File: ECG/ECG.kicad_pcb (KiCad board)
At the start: 4 copper layers, 151.1 x 116.2 mm, 51 parts, among them J1 Conn_01x03, J2 Conn_01x03, J3 Conn_01x15, J4 Conn_01x15, J5 Conn_01x02, Q1 DMG2301L, Q2 T2N7002AK, Q3 T2N7002AK, Q4 T2N7002AK, Q5 T2N7002AK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

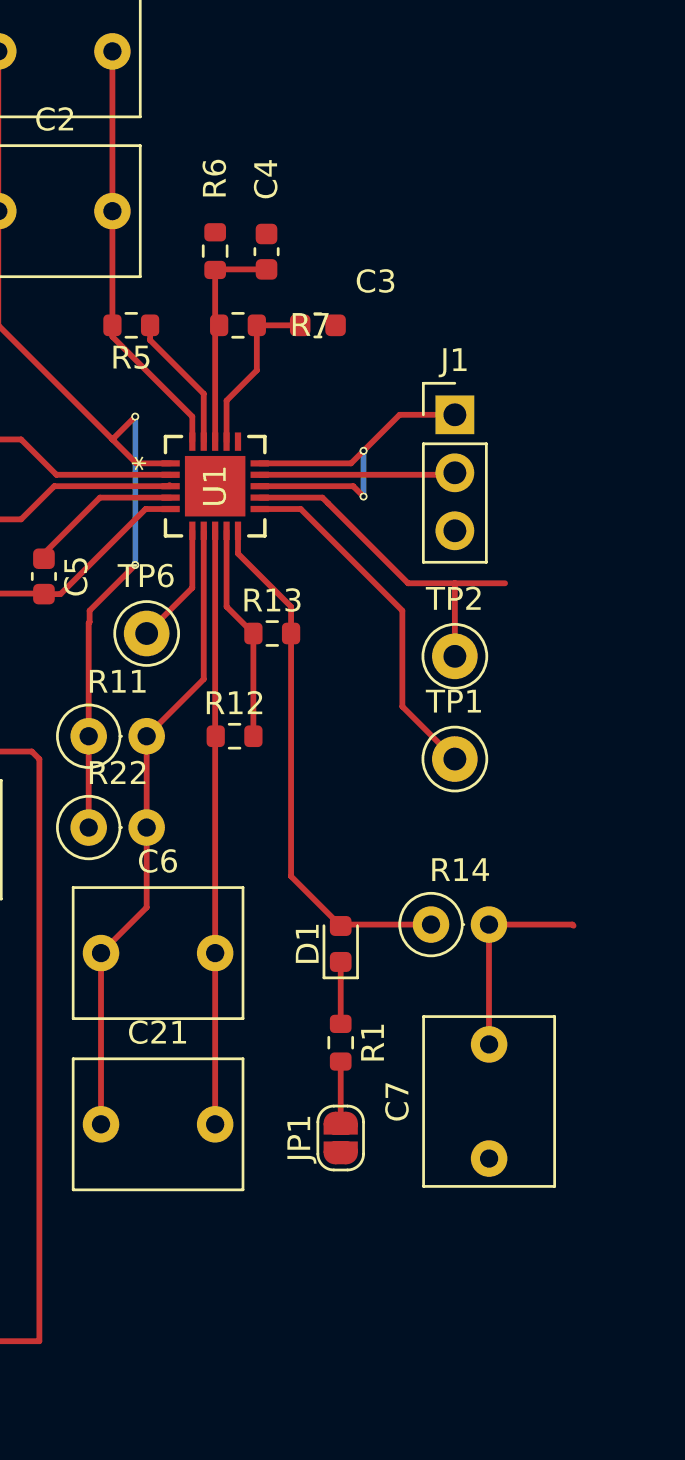
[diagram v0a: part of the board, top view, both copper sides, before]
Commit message: Vref, add TPs
Added R17, TP7, TP8
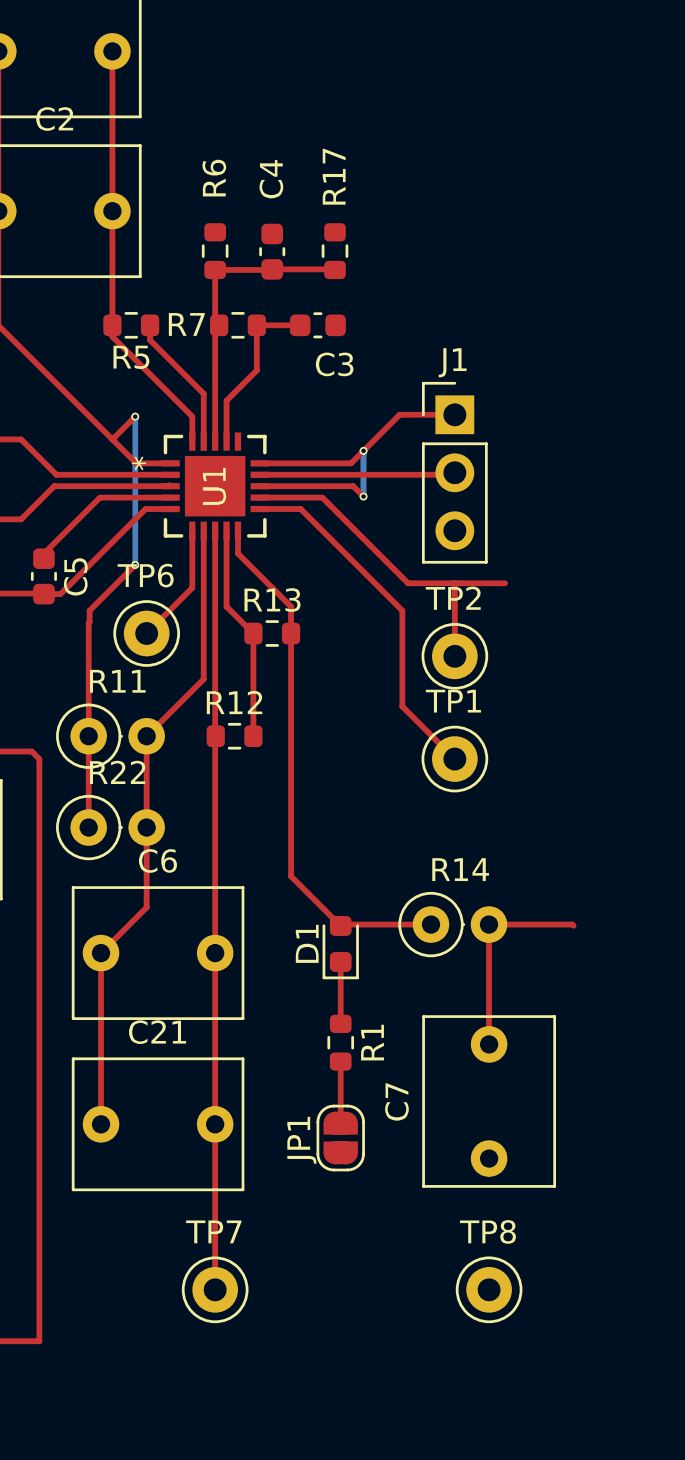
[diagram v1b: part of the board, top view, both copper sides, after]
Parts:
- added R17: 10M, Resistor_SMD:R_0603_1608Metric, F.Cu at (132.2, 62.8)
- added TP7: TestPoint, TestPoint:TestPoint_Keystone_5000-5004_Miniature, F.Cu at (127.0, 108.2)
- added TP8: TestPoint, TestPoint:TestPoint_Keystone_5000-5004_Miniature, F.Cu at (139.0, 108.2)
- moved C4 0.25 mm to (129.5, 62.8)
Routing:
- net Net-(U1-REFOUT): track 26.0 -> 33.3 mm
- net /VREFIN: track 9.85 -> 12.9 mm

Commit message: Labels
Added all labels
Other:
- board text added: "1.1v Vref"
- board text added: "2-WIRE"
- board text added: "3-WIRE"
- board text added: "3-WIRE DC"
- board text added: "AC 2-WIRE"
- board text added: "AD8232 ECG"
- board text added: "ANALOG OUTPUT"
- board text added: "GND"
- board text added: "HPF x100"
- board text added: "LEFT"
- board text added: "LOD+"
- board text added: "LOD-"
- board text added: "LPF1"
- board text added: "LPF2"
- board text added: "RIGHT"
- board text added: "RLD"
- board text added: "SW"
- board text added: "Vref"
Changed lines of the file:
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@@
 		(layer "Edge.Cuts")
+	)
+	(gr_text "3-WIRE"
+		(at 108.5 90.5 0)
+		(layer "F.SilkS")
+		(effects
+			(font
+				(size 1 1)
+				(thickness 0.1)
+			)
+			(justify left bottom)
+		)
+	)
+	(gr_text "AD8232\n ECG"
+		(at 106.75 54.25 0)
+		(layer "F.SilkS")
+		(effects
+			(font
+				(size 1 1)
+				(thickness 0.1)
+			)
+			(justify left bottom)
+		)
+	)
+	(gr_text "LPF2"
+		(at 136.13 95.5 0)
+		(layer "F.SilkS")
+		(effects
+			(font
+				(size 1 1)
+				(thickness 0.1)
+			)
+			(justify left bottom)
+		)
+	)
+	(gr_text "RLD"
+		(at 103.75 114 0)
+		(layer "F.SilkS")
+		(effects
+			(font
+				(size 1 1)
+				(thickness 0.1)
+			)
+			(justify left bottom)
+		)
+	)
+	(gr_text "3-WIRE\nDC"
+		(at 139.75 77 0)
+		(layer "F.SilkS")
+		(effects
+			(font
+				(size 1 1)
+				(thickness 0.1)
+			)
+			(justify left bottom)
+		)
+	)
+	(gr_text "ANALOG\nOUTPUT"
+		(at 140.25 93.75 0)
+		(layer "F.SilkS")
+		(effects
+			(font
+				(size 1 1)
+				(thickness 0.1)
+			)
+			(justify left bottom)
+		)
+	)
+	(gr_text "LEFT"
+		(at 104.5 64.75 0)
+		(layer "F.SilkS")
+		(effects
+			(font
+				(size 1 1)
+				(thickness 0.1)
+			)
+			(justify left bottom)
+		)
+	)
+	(gr_text "AC\n2-WIRE"
+		(at 139.5 70.5 0)
+		(layer "F.SilkS")
+		(effects
+			(font
+				(size 1 1)
+				(thickness 0.1)
+			)
+			(justify left bottom)
+		)
+	)
+	(gr_text "LOD-"
+		(at 139.5 85.25 0)
+		(layer "F.SilkS")
+		(effects
+			(font
+				(size 1 1)
+				(thickness 0.1)
+			)
+			(justify left bottom)
+		)
+	)
+	(gr_text "SW"
+		(at 120 80.25 0)
+		(layer "F.SilkS")
+		(effects
+			(font
+				(size 1 1)
+				(thickness 0.1)
+			)
+			(justify left bottom)
+		)
+	)
+	(gr_text "GND"
+		(at 137.75 112.5 0)
+		(layer "F.SilkS")
+		(effects
+			(font
+				(size 1 1)
+				(thickness 0.1)
+			)
+			(justify left bottom)
+		)
+	)
+	(gr_text "RIGHT"
+		(at 103.75 88.75 0)
+		(layer "F.SilkS")
+		(effects
+			(font
+				(size 1 1)
+				(thickness 0.1)
+			)
+			(justify left bottom)
+		)
+	)
+	(gr_text "LPF1"
+		(at 120.75 106 0)
+		(layer "F.SilkS")
+		(effects
+			(font
+				(size 1 1)
+				(thickness 0.1)
+			)
+			(justify left bottom)
+		)
+	)
+	(gr_text "LOD+"
+		(at 139.5 81 0)
+		(layer "F.SilkS")
+		(effects
+			(font
+				(size 1 1)
+				(thickness 0.1)
+			)
+			(justify left bottom)
+		)
+	)
+	(gr_text "HPF\nx100"
+		(at 112 62.25 0)
+		(layer "F.SilkS")
+		(effects
+			(font
+				(size 1 1)
+				(thickness 0.1)
+			)
+			(justify left bottom)
+		)
+	)
+	(gr_text "Vref"
+		(at 125.75 112.5 0)
+		(layer "F.SilkS")
+		(effects
+			(font
+				(size 1 1)
+				(thickness 0.1)
+			)
+			(justify left bottom)
+		)
+	)
+	(gr_text "1.1v\nVref"
+		(at 133.5 64.25 0)
+		(layer "F.SilkS")
+		(effects
+			(font
+				(size 1 1)
+				(thickness 0.1)
+			)
+			(justify left bottom)
+		)
+	)
+	(gr_text "2-WIRE"
+		(at 108.5 85.25 0)
+		(layer "F.SilkS")
+		(effects
+			(font
+				(size 1 1)
+				(thickness 0.1)
+			)
+			(justify left bottom)
+		)
 	)
 	(segment

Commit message: start cleanup
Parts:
- moved R11 14.1 mm to (135.3, 86.7)
- moved R22 14.1 mm to (135.3, 90.7)
- moved C4 14.1 mm to (143.4, 65.5)
- moved D1 14.1 mm to (146.4, 95.8)
- moved JP1 14.1 mm to (146.4, 104.3)
- moved C2 14.1 mm to (131.4, 63.7)
- moved C21 14.1 mm to (135.9, 103.7)
- moved C22 14.1 mm to (131.4, 56.7)
- moved C3 14.1 mm to (145.4, 68.7)
- moved C5 14.1 mm to (133.4, 79.7)
- moved C6 14.1 mm to (135.9, 96.2)
- moved C7 14.1 mm to (152.9, 105.2)
- moved J1 14.1 mm to (151.4, 72.6)
- moved J2 14.1 mm to (130.1, 87.4)
- moved R1 14.1 mm to (146.4, 100.1)
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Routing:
- net /FILTER_OUT: track 8.98 -> 33.0 mm

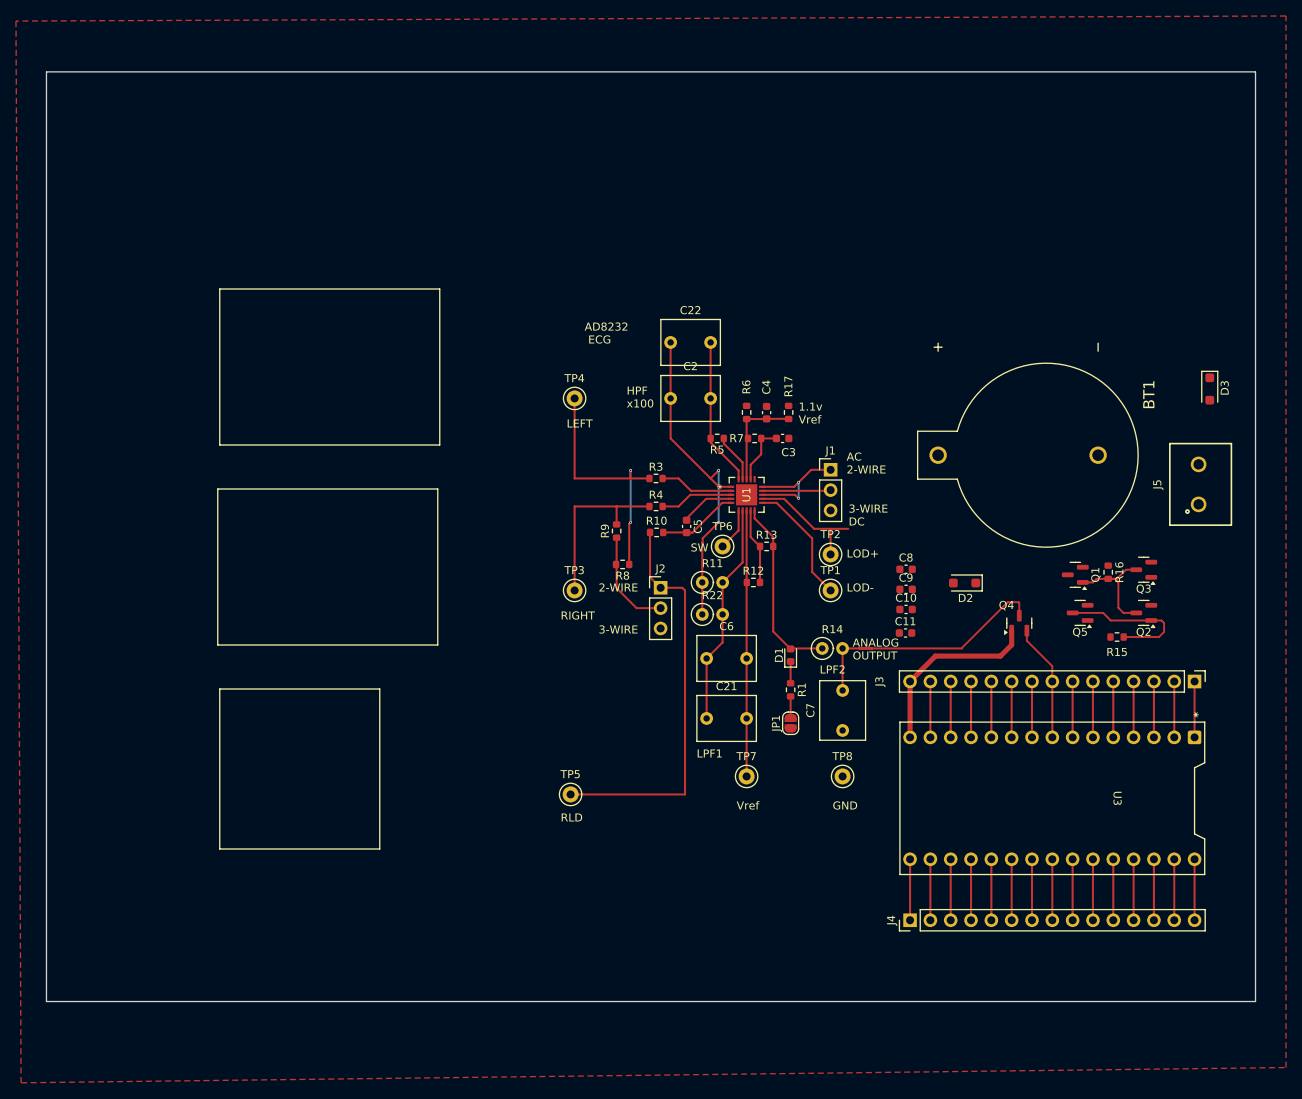
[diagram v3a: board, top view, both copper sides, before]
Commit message: WIP:
1) Cleanup macro placement a bit to reduce board cost.
2) Start final routing and plane additions
3) Clean up drcs.
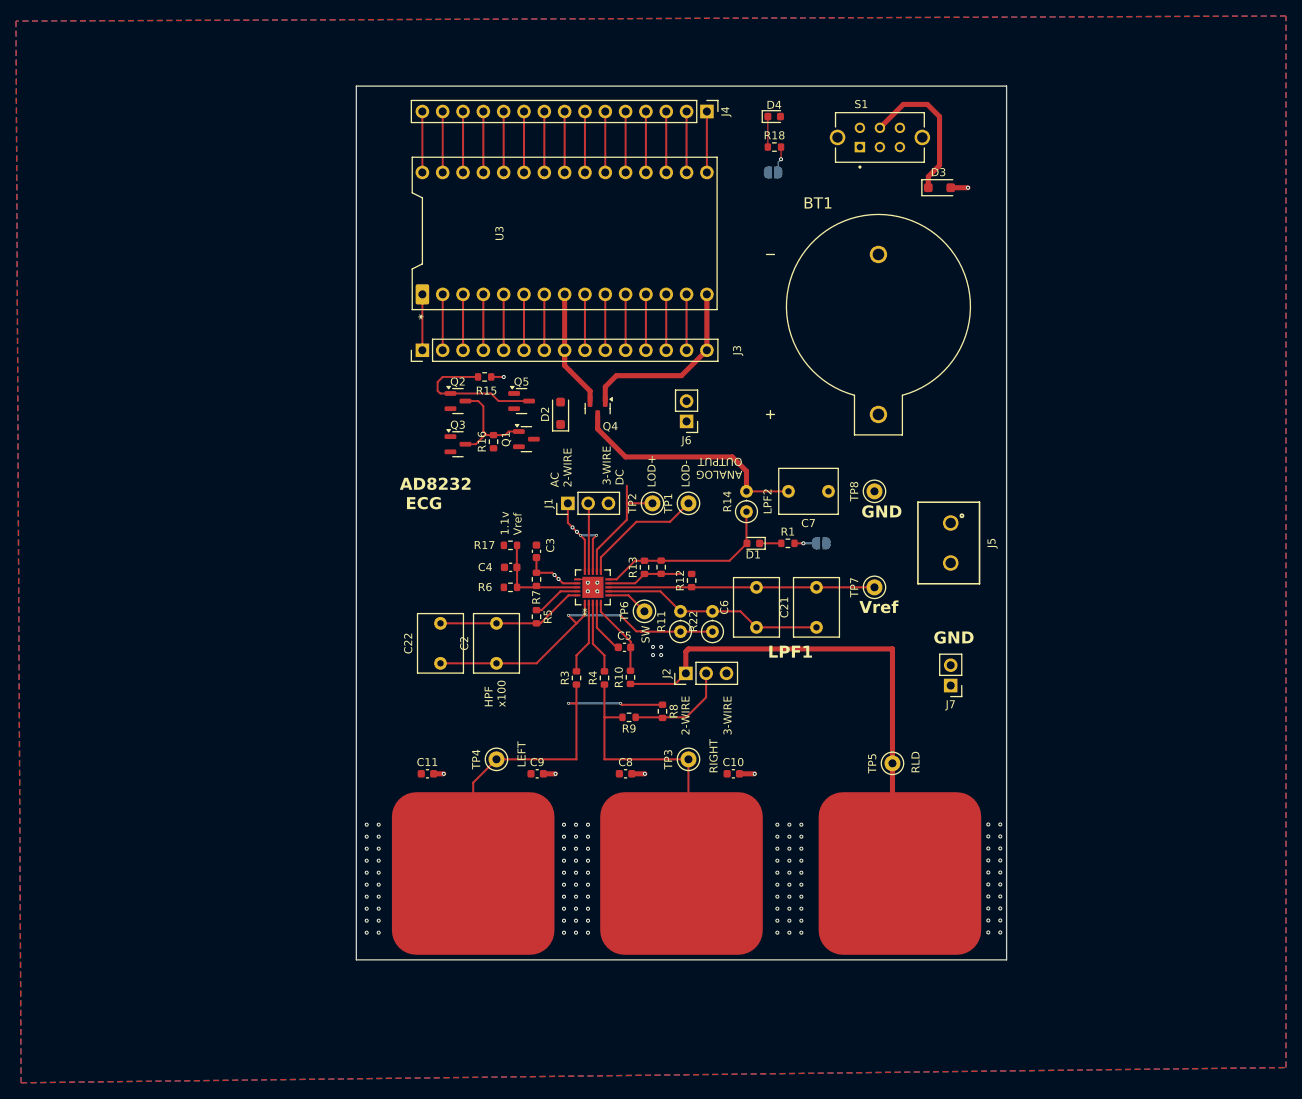
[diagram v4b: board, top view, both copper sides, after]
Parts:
- added D4: LED_Red, LED_SMD:LED_0603_1608Metric, F.Cu at (144.3, 28.4)
- added J6: Conn_01x02, Connector_PinHeader_2.54mm:PinHeader_1x02_P2.54mm_Vertical, F.Cu at (133.3, 66.6)
- added J7: Conn_01x02, Connector_PinHeader_2.54mm:PinHeader_1x02_P2.54mm_Vertical, F.Cu at (166.4, 99.6)
- added JP2: SolderJumper_2_Open, Jumper:SolderJumper-2_P1.3mm_Open_RoundedPad1.0x1.5mm, B.Cu at (144.2, 35.4)
- added R18: 6.8K, Resistor_SMD:R_0603_1608Metric, F.Cu at (144.3, 32.3)
- added R2: DNP, Resistor_SMD:R_0603_1608Metric, F.Cu at (130.2, 84.8)
- added S1: SLW-118562-4A-N-D, ECG_Footprints:SW_SLW-118562-4A-N-D, F.Cu at (157.5, 31.1)
- added TP10: TestPoint, ECG_Footprints:FingerPad, F.Cu at (132.7, 123.1)
- added TP11: TestPoint, ECG_Footprints:FingerPad, F.Cu at (106.7, 123.1)
- added TP9: TestPoint, ECG_Footprints:FingerPad, F.Cu at (160.0, 123.1)
- D3: value D_Schottky_Small_Filled -> ~
- JP1: moved to B.Cu
- moved J3 105.0 mm to (100.3, 57.7), turned to 90 degrees
- moved J4 104.2 mm to (135.9, 27.8), turned to -90 degrees
- moved U3 103.9 mm to (110.5, 43.1), turned to 90 degrees
- moved Q2 89.7 mm to (104.8, 64.0), turned to 0 degrees
- moved Q3 87.1 mm to (104.8, 69.4), turned to 0 degrees
- moved R15 85.5 mm to (108.1, 61.0), turned to 180 degrees
- moved R16 78.5 mm to (109.2, 69.1), turned to 90 degrees
- moved Q5 74.7 mm to (112.7, 64.0), turned to 0 degrees
- moved Q1 70.7 mm to (113.3, 68.8), turned to 0 degrees
- moved C11 62.3 mm to (101.0, 110.6)
- moved Q4 59.1 mm to (122.2, 64.9), turned to -90 degrees
- moved D2 54.8 mm to (117.6, 65.5), turned to 90 degrees
- moved C9 51.6 mm to (114.7, 110.6)
- moved C22 49.4 mm to (102.6, 96.8), turned to 90 degrees
- moved TP4 46.2 mm to (109.6, 108.8), turned to 90 degrees
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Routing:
- net Net-(D3-A): track 0.00 -> 45.0 mm, vias 0 -> 1
- net Net-(BT1-Pad+): track 0.00 -> 35.0 mm
- net Net-(D3-K): track 0.00 -> 18.8 mm
- net /INP: track 32.2 -> 47.6 mm
- net /INM: track 22.1 -> 37.1 mm
- net /RL: track 50.5 -> 64.6 mm
- net /HR_SIGNAL: track 14.7 -> 25.4 mm
- net +3V0: track 23.8 -> 31.6 mm, vias 2 -> 11
- net Net-(D4-K): track 0.00 -> 3.81 mm
- net Net-(JP2-B): track 0.00 -> 3.32 mm, vias 0 -> 1
- net /FILTER_OUT: track 33.0 -> 30.2 mm
- net GND: track 15.2 -> 16.2 mm, vias 0 -> 108
- net Net-(JP1-B): vias 0 -> 1
- added copper zone on In2.Cu, net +3V0
- added copper zone on B.Cu, net GND
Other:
- board size 151.1 x 116.2 mm -> 81.3 x 109.2 mm
- board text added: "+9V"

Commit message: DRC and ERC clean.
Decent layout.

Silk needs work.
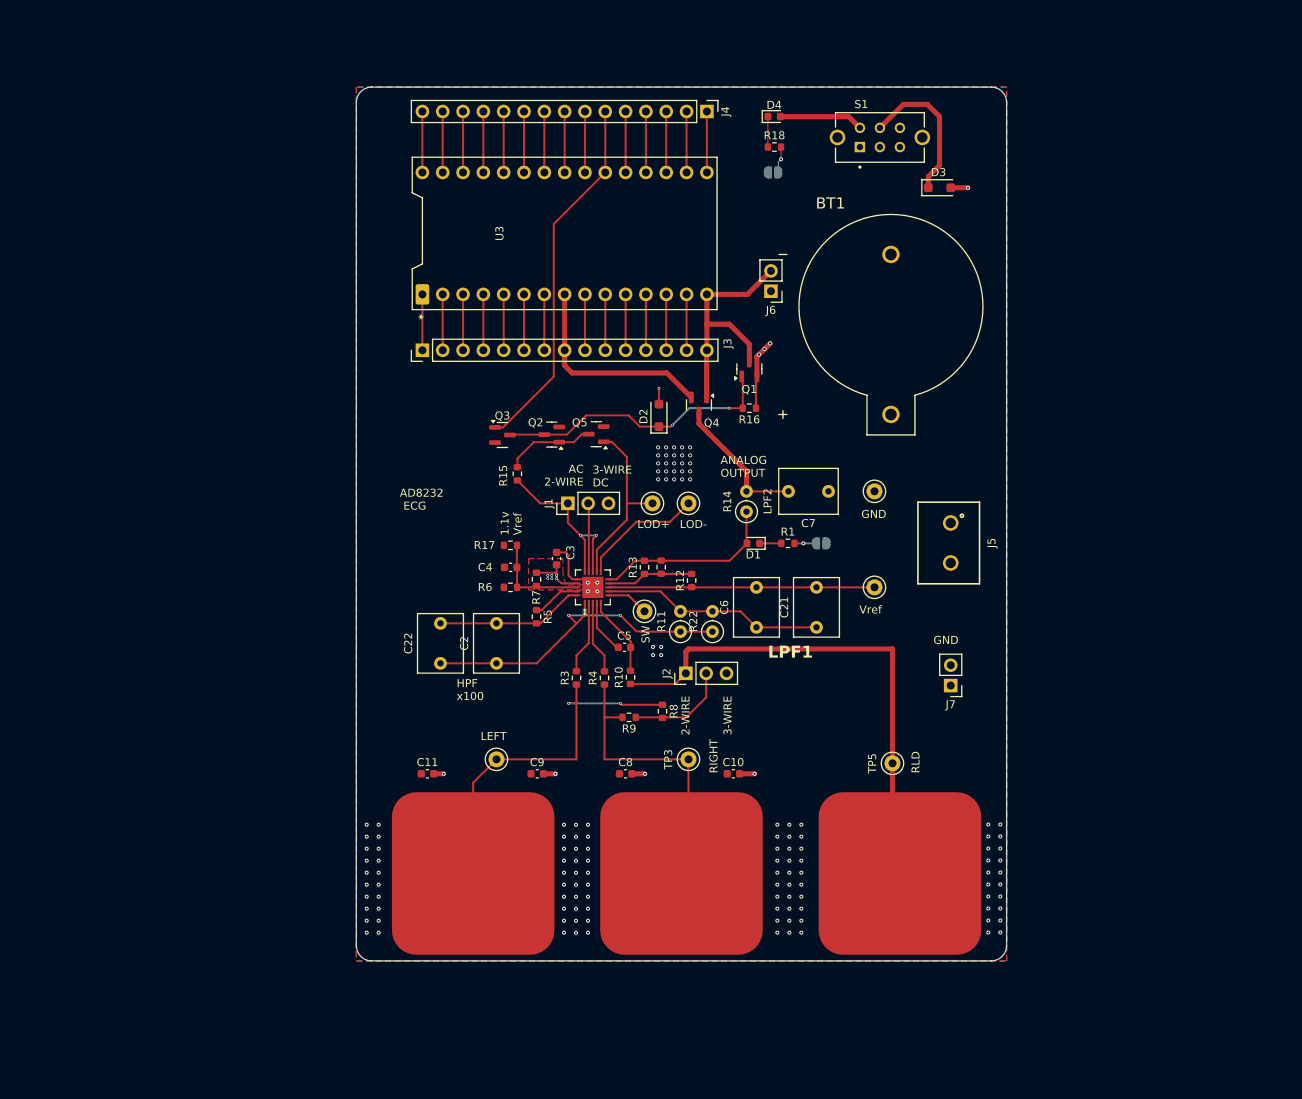
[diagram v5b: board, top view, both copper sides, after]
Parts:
- moved R16 32.3 mm to (141.2, 64.9), turned to 180 degrees
- moved Q1 29.2 mm to (141.2, 60.0), turned to 90 degrees
- moved J6 19.4 mm to (143.9, 50.3)
- moved R15 12.8 mm to (112.2, 73.1), turned to 90 degrees
- moved Q4 12.7 mm to (134.9, 64.5)
- moved Q2 12.5 mm to (116.5, 68.2), turned to 180 degrees
- moved D2 12.3 mm to (129.9, 65.8)
- moved Q5 10.2 mm to (122.1, 68.2), turned to 180 degrees
- moved Q3 5.68 mm to (110.3, 68.2)
- moved C3 2.67 mm to (117.1, 83.7)
- moved BT1 1.56 mm to (158.9, 52.2)
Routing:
- net +9V: track 0.00 -> 58.4 mm, vias 0 -> 3
- net /PWR_HOLD: track 7.62 -> 45.8 mm
- net /D2: track 7.62 -> 38.3 mm, vias 0 -> 1
- net /PWR_OFF_HV: track 14.5 -> 35.7 mm, vias 0 -> 2
- net /FILTER_OUT: track 30.2 -> 17.6 mm
- net /HR_SIGNAL: track 25.4 -> 37.2 mm
- net /VIN: track 23.4 -> 30.6 mm
- net /LODP: track 15.5 -> 22.8 mm
- net /PWR_ON: track 18.4 -> 11.3 mm
- net GND: track 16.2 -> 23.1 mm, vias 108 -> 133
- net +3V0: track 31.6 -> 37.1 mm, vias 11 -> 12
- net Net-(U1-OPAMP-): track 9.49 -> 10.9 mm
- added copper zone on F.Cu, net +3V0
- added copper zone on In1.Cu, net GND
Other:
- outline, holes or cut-outs redrawn
